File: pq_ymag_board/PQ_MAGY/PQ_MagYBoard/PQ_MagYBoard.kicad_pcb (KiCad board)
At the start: 6 copper layers, 45 x 45 mm, 10 parts, among them J1 M20-7810245

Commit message: Functional revision and finishing touches part II
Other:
- board text added: "Y Magnetorquer Board"

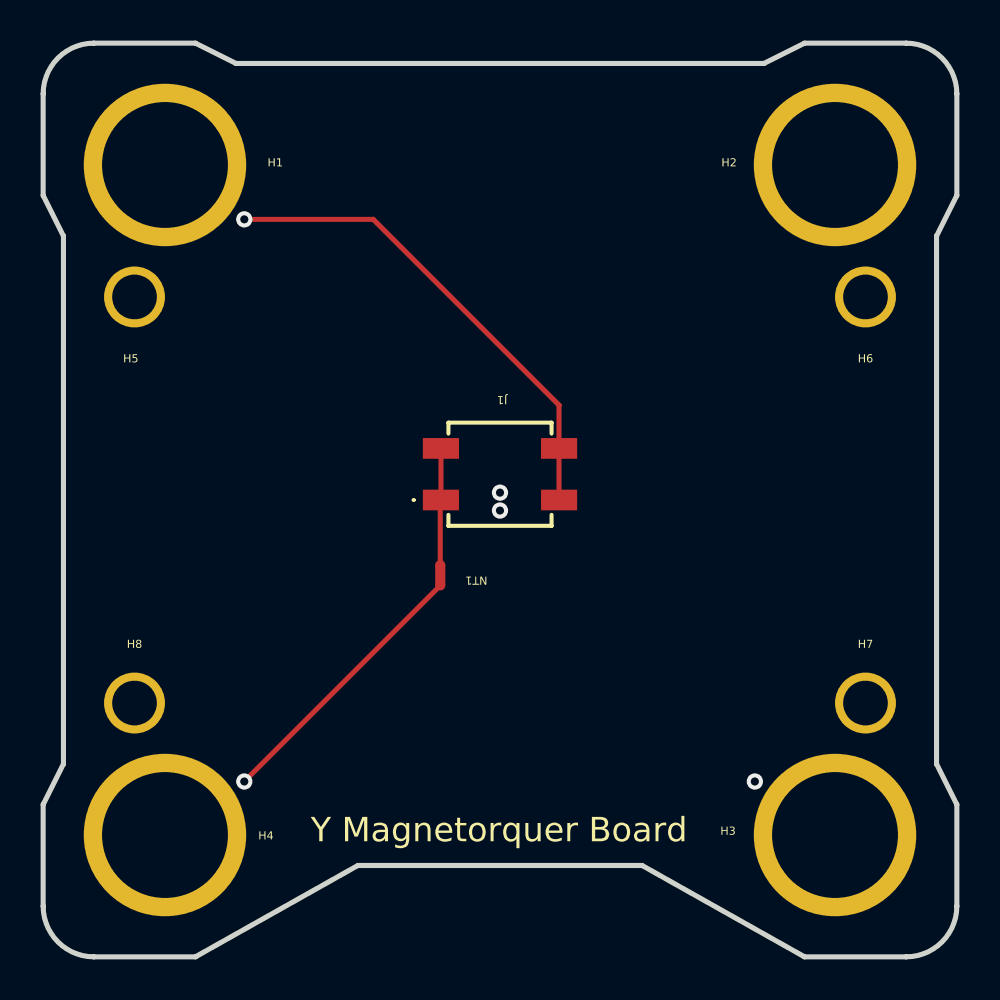
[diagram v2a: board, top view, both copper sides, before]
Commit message: Full Kicad7 transition, library improvement and adaptation, correct footprints and 3D models added
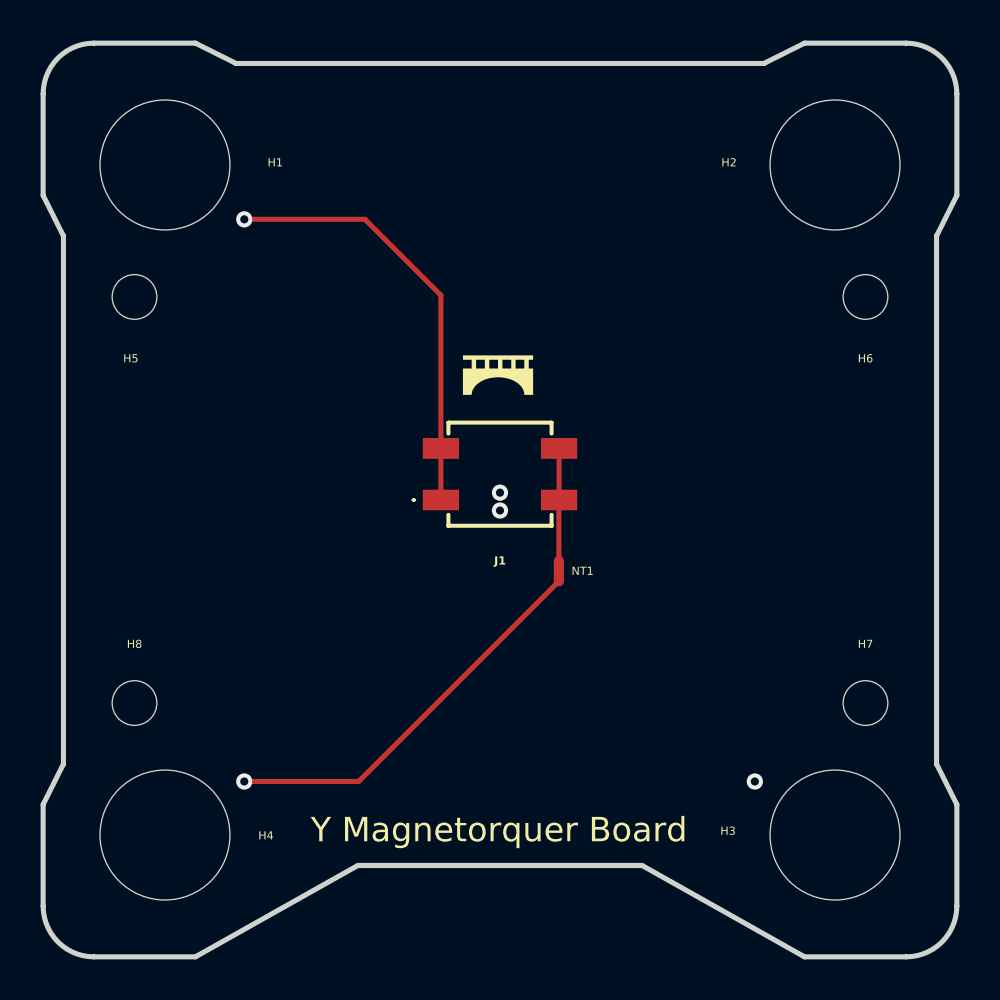
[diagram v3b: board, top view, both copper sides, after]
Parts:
- added Annotation1: Silkscreen_Annotation, -nsl_symbols:Bridgemaker, F.Cu at (101.6, 54.7)
- J1: footprint SamacSys_Parts:M207810245 -> -nsl_connector:M207810245
- moved NT1 5.85 mm to (104.6, 64.2)
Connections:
- J1 pad 1: /MAG+Y -> /VCC_MAG
- J1 pad 2: /VCC_MAG -> /MAG+Y
- J1 pad 3: /MAG+Y -> /VCC_MAG
- J1 pad 4: /VCC_MAG -> /MAG+Y
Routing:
- net /VCC_MAG: track 6366.8 -> 6370.0 mm

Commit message: step and files created for all subsystems
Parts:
- removed Annotation1: Silkscreen_Annotation, -nsl_symbols:Bridgemaker
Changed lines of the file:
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@@
     (property "ki_keywords" "mounting hole")
     (attr exclude_from_pos_files)
-    (fp_text reference "H8" (at 0 -2.9 unlocked) (layer "F.SilkS")
+    (fp_text reference "H8" (at 0 -2.9 unlocked) (layer "F.SilkS") hide
         (effects (font (size 0.4 0.4) (thickness 0.15)))
     )
@@
     (property "ki_keywords" "mounting hole")
     (attr exclude_from_pos_files)
-    (fp_text reference "H2" (at -5.218 -0.116 unlocked) (layer "F.SilkS")
+    (fp_text reference "H2" (at -5.218 -0.116 unlocked) (layer "F.SilkS") hide
         (effects (font (size 0.4 0.4) (thickness 0.1)))
     )
@@
     (property "ki_keywords" "mounting hole")
     (attr exclude_from_pos_files)
-    (fp_text reference "H1" (at 5.43 -0.116 unlocked) (layer "F.SilkS")
+    (fp_text reference "H1" (at 5.43 -0.116 unlocked) (layer "F.SilkS") hide
         (effects (font (size 0.4 0.4) (thickness 0.1)))
     )
@@
     (property "ki_keywords" "mounting hole")
     (attr exclude_from_pos_files)
-    (fp_text reference "H7" (at 0 -2.9 unlocked) (layer "F.SilkS")
+    (fp_text reference "H7" (at 0 -2.9 unlocked) (layer "F.SilkS") hide
         (effects (font (size 0.4 0.4) (thickness 0.15)))
     )
@@
     (property "ki_keywords" "mounting hole")
     (attr exclude_from_pos_files)
-    (fp_text reference "H5" (at -0.182 3.036 unlocked) (layer "F.SilkS")
+    (fp_text reference "H5" (at -0.182 3.036 unlocked) (layer "F.SilkS") hide
         (effects (font (size 0.4 0.4) (thickness 0.15)))
     )
@@
     (property "ki_keywords" "mounting hole")
     (attr exclude_from_pos_files)
-    (fp_text reference "H6" (at 0 3.036 unlocked) (layer "F.SilkS")
+    (fp_text reference "H6" (at 0 3.036 unlocked) (layer "F.SilkS") hide
         (effects (font (size 0.4 0.4) (thickness 0.15)))
     )
@@
     (property "ki_keywords" "mounting hole")
     (attr exclude_from_pos_files)
-    (fp_text reference "H4" (at 4.9728 0.031 unlocked) (layer "F.SilkS")
+    (fp_text reference "H4" (at 4.9728 0.031 unlocked) (layer "F.SilkS") hide
         (effects (font (size 0.4 0.4) (thickness 0.1)))
     )
@@
     (property "ki_keywords" "mounting hole")
     (attr exclude_from_pos_files)
-    (fp_text reference "H3" (at -5.2688 -0.1976 unlocked) (layer "F.SilkS")
-        (effects (font (size 0.4 0.4) (thickness 0.1)))
-    )
-    (fp_text value "MountingHole" (at 0 6.5) (layer "F.Fab") hide
-        (effects (font (size 1 1) (thickness 0.15)))
-    )
-    (fp_text user "${REFERENCE}" (at 0 0) (layer "F.Fab")
-        (effects (font (size 1 1) (thickness 0.15)))
-    )
-    (fp_circle (center 0 0) (end 4 0)
-      (stroke (width 0.15) (type solid)) (fill none) (layer "Cmts.User"))
-    (fp_circle (center 0 0) (end 4 0)
-      (stroke (width 0.05) (type solid)) (fill none) (layer "F.CrtYd"))
-    (pad "" np_thru_hole circle (at 0 0) (size 6.4 6.4) (drill 6.4) (layers "*.Cu" "*.Mask"))
-  )
-  (footprint "-nsl_symbols:Bridgemaker" (layer "F.Cu")
-    (at 101.604931 54.686381)
-    (property "Sheetfile" "PQ_MagYBoard.kicad_sch")
-    (property "Sheetname" "")
-    (attr smd)
-    (fp_text reference "Annotation1" (at 0 -0.5 unlocked) (layer "F.SilkS") hide
-        (effects (font (size 1 1) (thickness 0.15)))
-    )
-    (fp_text value "Silkscreen_Annotation" (at 0 1.905 unlocked) (layer "F.Fab")
-        (effects (font (size 1 1) (thickness 0.15)))
-    )
-    (fp_text user "${REFERENCE}" (at 0 3.175 unlocked) (layer "F.Fab")
-        (effects (font (size 1 1) (thickness 0.15)))
-    )
-    (fp_poly
-      (pts
-        (xy 1.77448 -0.846525)
-        (xy 1.559286 -0.846525)
-        (xy 1.559286 -0.416136)
-        (xy 1.77448 -0.416136)
-        (xy 1.77448 0.882086)
-        (xy 1.55858 0.881381)
-        (xy 1.342327 0.880322)
-        (xy 1.339858 0.839753)
-        (xy 1.338186 0.818605)
-        (xy 1.335689 0.797501)
-        (xy 1.328251 0.75547)
-        (xy 1.317606 0.71375)
-        (xy 1.303819 0.672431)
-        (xy 1.286952 0.631602)
-        (xy 1.267069 0.591353)
-        (xy 1.244231 0.551771)
-        (xy 1.218502 0.512948)
-        (xy 1.189946 0.474973)
-        (xy 1.158625 0.437934)
-        (xy 1.124603 0.401922)
-        (xy 1.087941 0.367025)
-        (xy 1.048705 0.333334)
-        (xy 1.006955 0.300936)
-        (xy 0.962757 0.269923)
-        (xy 0.916172 0.240383)
-        (xy 0.882037 0.220457)
-        (xy 0.847108 0.201427)
-        (xy 0.811392 0.183295)
-        (xy 0.774895 0.166063)
-        (xy 0.737625 0.149735)
-        (xy 0.69959 0.134312)
-        (xy 0.660795 0.119798)
-        (xy 0.621249 0.106196)
-        (xy 0.58096 0.093506)
-        (xy 0.539933 0.081733)
-        (xy 0.498176 0.070879)
-        (xy 0.455698 0.060946)
-        (xy 0.412503 0.051937)
-        (xy 0.368601 0.043855)
-        (xy 0.323999 0.036702)
-        (xy 0.278702 0.030481)
-        (xy 0.219963 0.024359)
-        (xy 0.156851 0.020267)
-        (xy 0.090745 0.018184)
-        (xy 0.023027 0.018089)
-        (xy -0.044923 0.019963)
-        (xy -0.111723 0.023783)
-        (xy -0.175994 0.029531)
-        (xy -0.236353 0.037183)
-        (xy -0.326021 0.052787)
-        (xy -0.413087 0.072497)
-        (xy -0.497298 0.096147)
-        (xy -0.578399 0.12357)
-        (xy -0.656137 0.154597)
-        (xy -0.693665 0.171411)
-        (xy -0.730258 0.189063)
-        (xy -0.765883 0.207532)
-        (xy -0.800508 0.226798)
-        (xy -0.834103 0.246839)
-        (xy -0.866635 0.267636)
-        (xy -0.898072 0.289166)
-        (xy -0.928383 0.311409)
-        (xy -0.957536 0.334343)
-        (xy -0.985499 0.357949)
-        (xy -1.012242 0.382205)
-        (xy -1.03773 0.407091)
-        (xy -1.061935 0.432584)
-        (xy -1.084822 0.458665)
-        (xy -1.106362 0.485312)
-        (xy -1.126521 0.512504)
-        (xy -1.145269 0.540221)
-        (xy -1.162573 0.568442)
-        (xy -1.178403 0.597145)
-        (xy -1.192725 0.62631)
-        (xy -1.205509 0.655916)
-        (xy -1.216723 0.685942)
-        (xy -1.223324 0.705863)
-        (xy -1.229119 0.725453)
-        (xy -1.234129 0.744778)
-        (xy -1.238374 0.763906)
-        (xy -1.241875 0.7829)
-        (xy -1.244653 0.801829)
-        (xy -1.246727 0.820758)
-        (xy -1.24812 0.839753)
-        (xy -1.250589 0.880322)
-        (xy -1.466489 0.881381)
-        (xy -1.682742 0.882086)
-        (xy -1.682742 -0.416136)
-        (xy -1.252353 -0.416136)
-        (xy -1.033631 -0.416136)
-        (xy -0.603242 -0.416136)
-        (xy -0.38452 -0.416136)
-        (xy 0.045869 -0.416136)
-        (xy 0.261063 -0.416136)
-        (xy 0.69498 -0.416136)
-        (xy 0.910175 -0.416136)
-        (xy 1.340563 -0.416136)
-        (xy 1.340563 -0.846525)
-        (xy 0.910175 -0.846525)
-        (xy 0.910175 -0.416136)
-        (xy 0.69498 -0.416136)
-        (xy 0.69498 -0.846525)
-        (xy 0.261063 -0.846525)
-        (xy 0.261063 -0.416136)
-        (xy 0.045869 -0.416136)
-        (xy 0.045869 -0.846525)
-        (xy -0.38452 -0.846525)
-        (xy -0.38452 -0.416136)
-        (xy -0.603242 -0.416136)
-        (xy -0.603242 -0.846525)
-        (xy -1.033631 -0.846525)
-        (xy -1.033631 -0.416136)
-        (xy -1.252353 -0.416136)
-        (xy -1.252353 -0.846525)
-        (xy -1.682742 -0.846525)
-        (xy -1.682742 -1.065247)
-        (xy 1.77448 -1.065247)
-      )
-      (stroke (width 0) (type solid)) (fill solid) (layer "F.SilkS"))
-    (group "" (id 7f891a7e-8086-4f51-9453-8485740a97a1)
-      (members
-        4e35cbc6-e929-4a63-a8f5-d10249238c39
-      )
-    )
+    (fp_text reference "H3" (at -5.2688 -0.1976 unlocked) (layer "F.SilkS") hide
+        (effects (font (size 0.4 0.4) (thickness 0.1)))
+    )
+    (fp_text value "MountingHole" (at 0 6.5) (layer "F.Fab") hide
+        (effects (font (size 1 1) (thickness 0.15)))
+    )
+    (fp_text user "${REFERENCE}" (at 0 0) (layer "F.Fab")
+        (effects (font (size 1 1) (thickness 0.15)))
+    )
+    (fp_circle (center 0 0) (end 4 0)
+      (stroke (width 0.15) (type solid)) (fill none) (layer "Cmts.User"))
+    (fp_circle (center 0 0) (end 4 0)
+      (stroke (width 0.05) (type solid)) (fill none) (layer "F.CrtYd"))
+    (pad "" np_thru_hole circle (at 0 0) (size 6.4 6.4) (drill 6.4) (layers "*.Cu" "*.Mask"))
   )
   (footprint "NetTie:NetTie-2_SMD_Pad0.5mm" (layer "F.Cu")
